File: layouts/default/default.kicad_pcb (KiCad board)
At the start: 2 copper layers, 37 parts

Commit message: Add modular design blocks and placement automation
- Add 8 modular sensor/power blocks in elec/modules/ for better layout
  organization (LIS3DHTR, QMI8658C, HDC2080, power filter, RF matching,
  I2C bus, status LED, NTC temp sensor)
- Add autoplace_v2.py with KiCad Python API and force-directed placement
- Add placement_config.yaml and block_templates.yaml for placement tuning
- Update main design to use modular block architecture
- Clean up old example build artifacts
- Remove unused patch_transformers.py

Co-Authored-By: Claude Opus 4.5 <noreply@anthropic.com>
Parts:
- B1: moved to B.Cu
- C1: value 5.6pF 50V C0G -> 1µF ±10% 50V X5R; footprint Murata_Electronics_GJM1555C1H5R6BB01D:C0402 -> Samsung_Electro_Mechanics_CL10A105KB8NNNC:C0603
- C10: value 1.7pF 50V C0G -> 100nF ±10% 50V X7R; footprint Murata_Electronics_GJM1555C1H1R7BB01D:C0402 -> YAGEO_CC0402KRX7R9BB104:C0402
- C11, C8: value 100nF ±10% 50V X7R -> 4.7µF ±10% 10V X5R; footprint YAGEO_CC0402KRX7R9BB104:C0402 -> Murata_Electronics_GRM155R61A475KEAAD:C0402
- C13: value 1µF ±10% 50V X5R -> 1.7pF 50V C0G; footprint Samsung_Electro_Mechanics_CL10A105KB8NNNC:C0603 -> Murata_Electronics_GJM1555C1H1R7BB01D:C0402
- C15, C16: value 100nF ±10% 50V X7R -> 5.6pF 50V C0G; footprint YAGEO_CC0402KRX7R9BB104:C0402 -> Murata_Electronics_GJM1555C1H5R6BB01D:C0402
- C2: value 5.6pF 50V C0G -> 100nF ±10% 50V X7R; footprint Murata_Electronics_GJM1555C1H5R6BB01D:C0402 -> YAGEO_CC0402KRX7R9BB104:C0402
- C3: value 4.7µF ±10% 10V X5R -> 100nF ±10% 50V X7R; footprint Murata_Electronics_GRM155R61A475KEAAD:C0402 -> YAGEO_CC0402KRX7R9BB104:C0402
- C6: value 4.7µF ±10% 10V X5R -> 22µF ±20% 6.3V X5R; footprint Murata_Electronics_GRM155R61A475KEAAD:C0402 -> YAGEO_CC0603MRX5R5BB226:C0603
- C9: value 22µF ±20% 6.3V X5R -> 100nF ±10% 50V X7R; footprint YAGEO_CC0603MRX5R5BB226:C0603 -> YAGEO_CC0402KRX7R9BB104:C0402
- L5: value 4.3nH 6GHz 750mA 140mΩ -> 4.7µH ±5% 175mA 2.3Ω; footprint Murata_Electronics_LQG15HS4N3S02D:L0402 -> TDK_NLV25T_4R7J_PF:IND-SMD_L2.5-W2.0_NLV25T-390J-PF
- L6: value 4.7µH ±5% 175mA 2.3Ω -> 4.3nH 6GHz 750mA 140mΩ; footprint TDK_NLV25T_4R7J_PF:IND-SMD_L2.5-W2.0_NLV25T-390J-PF -> Murata_Electronics_LQG15HS4N3S02D:L0402
- R1: value 10kΩ ±1% 62.5mW -> 4.7kΩ ±5% 62.5mW; footprint YAGEO_RC0402FR_0710KL:R0402 -> YAGEO_RC0402JR_074K7L:R0402
- R2: value (none) -> 4.7kΩ ±5% 62.5mW; footprint Murata_Electronics_NCP15XH103F03RC:R0402 -> YAGEO_RC0402JR_074K7L:R0402
- R3: value 10kΩ ±1% 62.5mW -> 1kΩ ±5% 62.5mW; footprint YAGEO_RC0402FR_0710KL:R0402 -> YAGEO_RC0402JR_071KL:R0402
- R4: value 1kΩ ±5% 62.5mW -> 10kΩ ±1% 62.5mW; footprint YAGEO_RC0402JR_071KL:R0402 -> YAGEO_RC0402FR_0710KL:R0402
- R5: value 4.7kΩ ±5% 62.5mW -> (none); footprint YAGEO_RC0402JR_074K7L:R0402 -> Murata_Electronics_NCP15XH103F03RC:R0402
- R6: value 4.7kΩ ±5% 62.5mW -> 10kΩ ±1% 62.5mW; footprint YAGEO_RC0402JR_074K7L:R0402 -> YAGEO_RC0402FR_0710KL:R0402
- U3: footprint Texas_Instruments_HDC2080DMBR:WSON-6_L3.0-W3.0-P1.00-TL-EP -> STMicroelectronics_LIS3DHTR:LGA-16_L3.0-W3.0-P0.50-TL
- U4: footprint STMicroelectronics_LIS3DHTR:LGA-16_L3.0-W3.0-P0.50-TL -> Texas_Instruments_HDC2080DMBR:WSON-6_L3.0-W3.0-P1.00-TL-EP
- moved L1 265.3 mm to (126.6, 73.2)
- moved R2 212.1 mm to (30.0, -10.0)
- moved C14 191.8 mm to (144.4, 86.2)
- moved R1 172.6 mm to (30.0, 0.00)
- moved U1 128.7 mm to (104.0, 75.7)
- moved B1 128.3 mm to (103.6, 75.7)
- moved H1 123.0 mm to (103.7, 66.1), turned to 180 degrees
- moved U2 117.3 mm to (68.8, 25.0)
- moved L2 86.0 mm to (70.0, -70.0)
- moved L3 86.0 mm to (70.0, -80.0)
- moved L4 86.0 mm to (70.0, -90.0)
- moved C15 85.4 mm to (80.0, -20.0)
- moved C16 85.4 mm to (80.0, -30.0)
- moved C13 82.5 mm to (80.0, -10.0)
- moved L6 82.5 mm to (80.0, -50.0)
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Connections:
- net footprint-CS-1 renamed footprint-CS
- net footprint-INT2-0 renamed footprint-int2
- C1 pad 1: c_harm-net -> accel-vcc
- C10 pad 1: c_harm-net -> accel-vcc
- C11 pad 1: c5-vcc -> c_vcc_1-vcc
- C12 pad 1: c5-vcc -> c_vcc_1-vcc
- C13 pad 1: c5-vcc -> c_harmonic-net
- C15 pad 1: c5-vcc -> Feed
- C16 pad 1: c5-vcc -> c_harmonic-net
- C2 pad 1: Feed -> accel-vcc
- C3 pad 1: c1-vcc -> accel-vcc
- C4 pad 1: c1-vcc -> accel-vcc
- C5 pad 1: vcc_mcu -> accel-vcc
- C6 pad 1: vcc_mcu -> vbat
- C7 pad 1: c5-vcc -> vcc_mcu
- C8 pad 1: c5-vcc -> vcc_mcu
- C9 pad 1: vbat -> accel-vcc
- H1 pad 1: c1-vcc -> c_vcc_1-vcc
- L2 pad 2: c1-vcc -> c_vcc_1-vcc
- L3 pad 1: c1-vcc -> c_vcc_1-vcc
- L4 pad 1: c1-vcc -> c_vcc_1-vcc
- L4 pad 2: c5-vcc -> accel-vcc
- L5 pad 1: c_harm-net -> RF_OUT
- L5 pad 2: Feed -> c_harmonic-net
- L6 pad 1: RF_OUT -> c_harmonic-net
- L6 pad 2: c_harm-net -> Feed
- R1 pad 1: c1-vcc -> c_vcc_1-vcc
- R1 pad 2: adc_ntc -> i2c_scl
- R2 pad 1: adc_ntc -> c_vcc_1-vcc
- R2 pad 2: gnd -> i2c_sda
- R3 pad 1: c1-vcc -> gpio_in
- R3 pad 2: activation -> A
- R4 pad 1: led_status -> c_vcc_1-vcc
- R4 pad 2: A -> adc_ntc
- R5 pad 1: c1-vcc -> adc_ntc
- R5 pad 2: i2c_sda -> gnd
- R6 pad 1: c1-vcc -> c_vcc_1-vcc
- R6 pad 2: i2c_scl -> activation
- U1 pad 14: footprint-INT2-1 -> accel-int2
- U1 pad 15: INT1 -> int1
- U1 pad 16: led_status -> gpio_in
- U1 pad 19: DRDY_INT -> int_pin
- U2 pad 4: c5-vcc -> accel-vcc
- U3 pad 1: i2c_sda -> accel-vcc
- U3 pad 2: gnd -> accel-net-0
- U3 pad 3: gnd -> accel-net-1
- U3 pad 4: DRDY_INT -> i2c_scl
- U3 pad 5: c5-vcc -> gnd
- U3 pad 6: i2c_scl -> i2c_sda
- U4 pad 1: c5-vcc -> i2c_sda
- U4 pad 2: footprint-net-4 -> gnd
- U4 pad 3: footprint-net-5 -> gnd
- U4 pad 4: i2c_scl -> int_pin
- U4 pad 5: gnd -> accel-vcc
- U4 pad 6: i2c_sda -> i2c_scl
- U5 pad 5: c5-vcc -> accel-vcc
- U5 pad 8: c5-vcc -> accel-vcc
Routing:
- net nrst: track 0.00 -> 17.7 mm
- net swdio: track 0.00 -> 11.2 mm
- net swclk: track 0.00 -> 10.9 mm
- net (no net): track 0.00 -> 10.5 mm

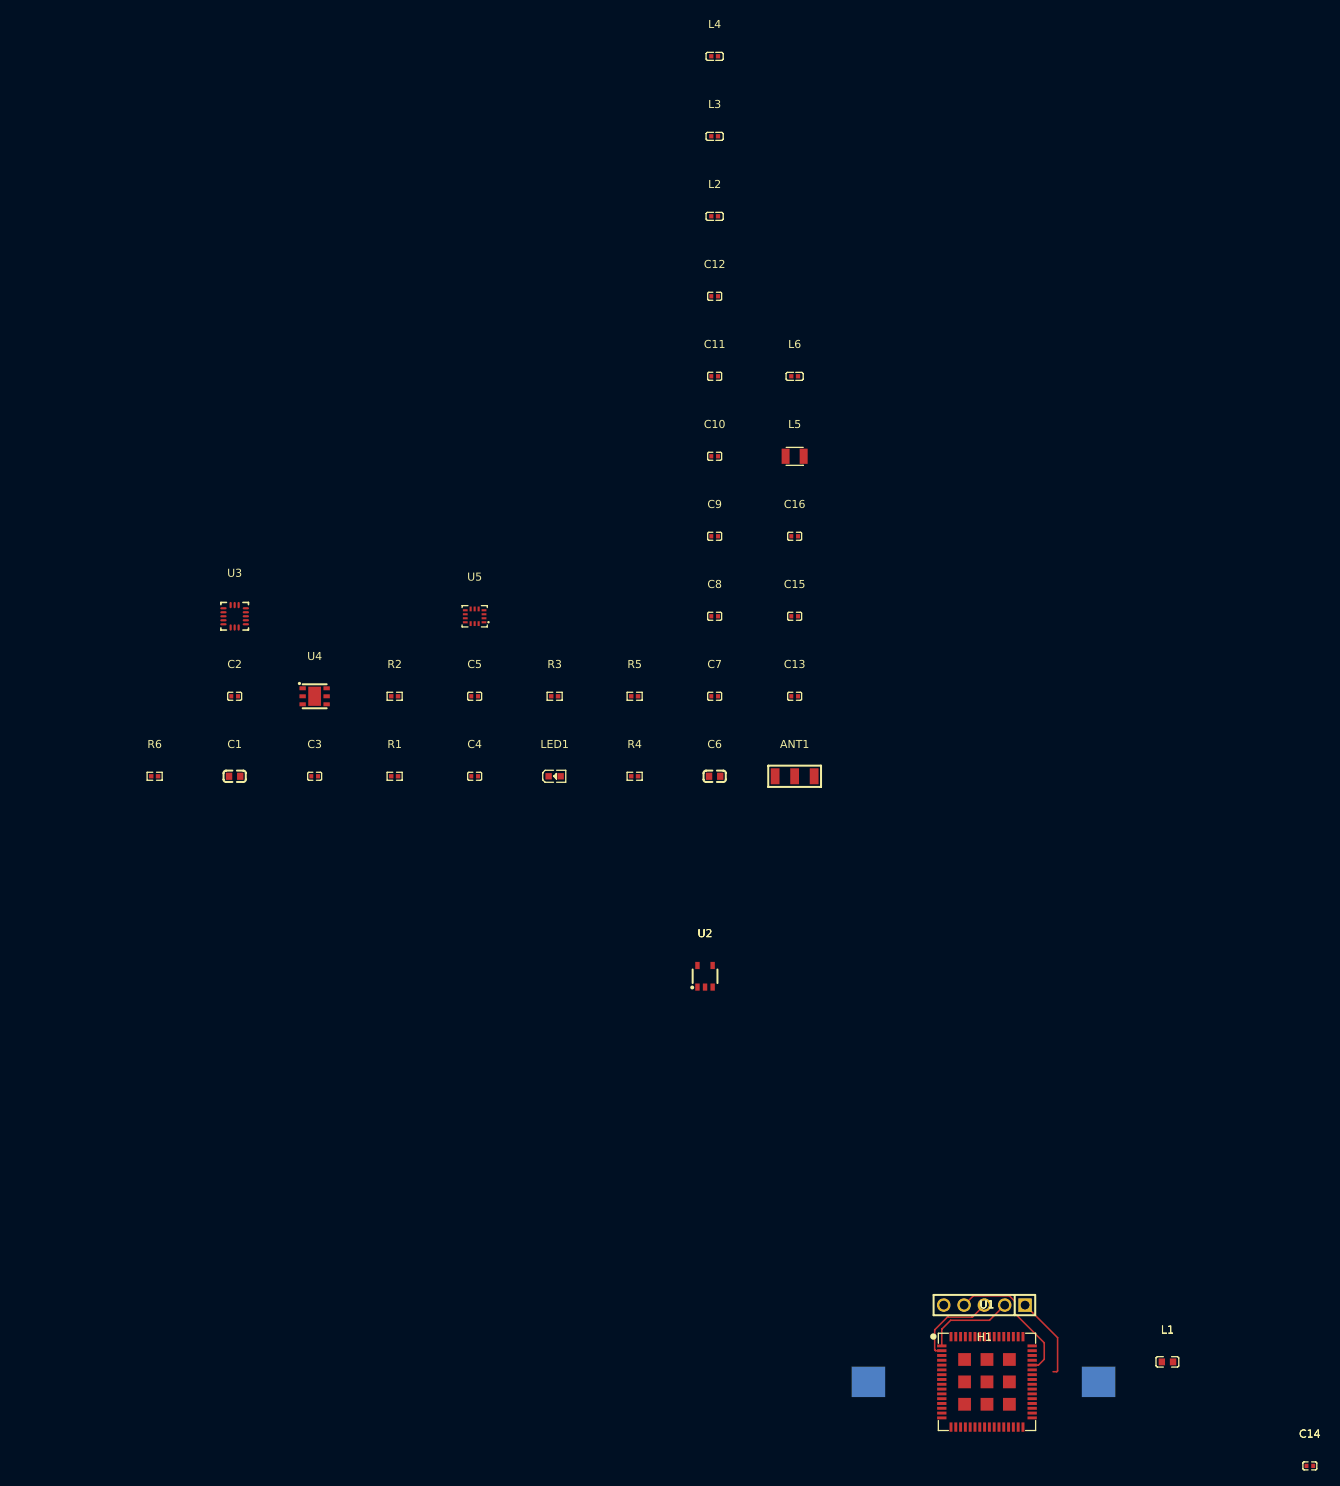
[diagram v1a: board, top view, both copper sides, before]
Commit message: Enhance smart placer with simulated annealing and pre-routing validation
Smart Placer improvements:
- Add simulated annealing refinement (now default) for better wire length optimization
- Add force-directed refinement with improvement safeguard
- Add silkscreen text repositioning to avoid component overlaps
- Significant wire length reductions (e.g., power_filter: 113mm -> 46mm)

Autorouter improvements:
- Add PreRoutingValidator class for pre-flight checks
- Validate unconnected pads, overlapping footprints, unplaced components
- Use pad-based bounds for accurate overlap detection
- Block routing on validation errors with actionable messages

Research:
- Add comprehensive autorouting/autoplacement findings document
- Cover Freerouting Python client, OrthoRoute, DeepPCB, KiCad 9 IPC API
- Document force-directed and simulated annealing algorithms

Cleanup:
- Update .gitignore for DSN/SES files, build artifacts, tools
- Remove stale timestamped build files
- Add parts footprints and symbols

All 10 modules placed and routed successfully.

Co-Authored-By: Claude Opus 4.5 <noreply@anthropic.com>
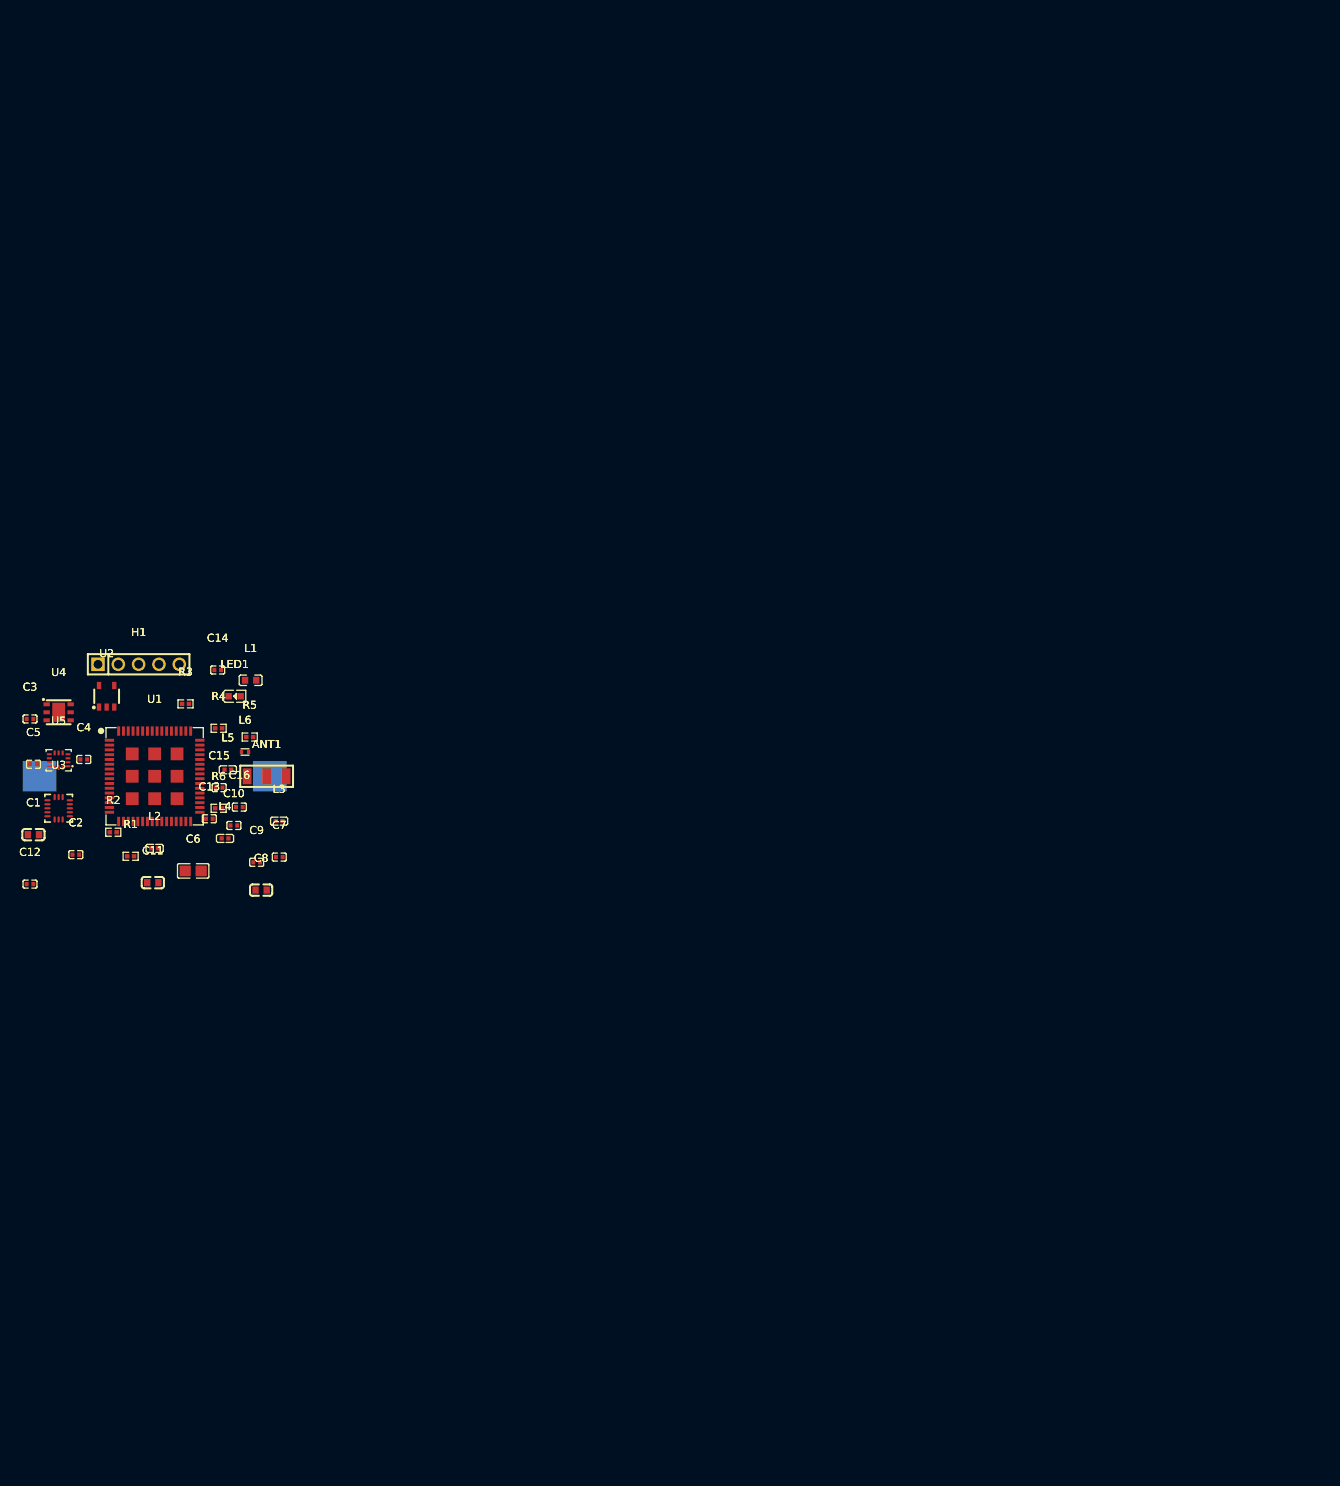
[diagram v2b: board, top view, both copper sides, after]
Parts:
- C1: value 1µF ±10% 50V X5R -> 10µF ±10% 10V X5R; footprint Samsung_Electro_Mechanics_CL10A105KB8NNNC:C0603 -> Samsung_Electro_Mechanics_CL10A106KP8NNNC:C0603
- C10, C12, C14, C2, C3, C4, C5, C7, C9: value 100nF ±10% 50V X7R -> 100nF ±10% 16V X7R; footprint YAGEO_CC0402KRX7R9BB104:C0402 -> Samsung_Electro_Mechanics_CL05B104KO5NNNC:C0402
- C11, C8: value 4.7µF ±10% 10V X5R -> 4.7µF ±10% 16V X5R; footprint Murata_Electronics_GRM155R61A475KEAAD:C0402 -> Samsung_Electro_Mechanics_CL10A475KO8NNNC:C0603
- C13: value 1.7pF 50V C0G -> 3.3pF ±2% 50V C0G; footprint Murata_Electronics_GJM1555C1H1R7BB01D:C0402 -> Murata_Electronics_GCM1555C1H3R3GA16D:C0402
- C15, C16: value 5.6pF 50V C0G -> (none)
- C6: value 22µF ±20% 6.3V X5R -> 22µF ±20% 25V X5R; footprint YAGEO_CC0603MRX5R5BB226:C0603 -> Samsung_Electro_Mechanics_CL21A226MAQNNNE:C0805
- L5: value 4.7µH ±5% 175mA 2.3Ω -> 8.2nH ±5% 3.6GHz 300mA 400mΩ; footprint TDK_NLV25T_4R7J_PF:IND-SMD_L2.5-W2.0_NLV25T-390J-PF -> Sunlord_SDCL1005C8N2JTDF:L0402
- L6: value 4.3nH 6GHz 750mA 140mΩ -> 4.2nH ±2% 1.8A 44mΩ; footprint Murata_Electronics_LQG15HS4N3S02D:L0402 -> Murata_Electronics_LQW15AN4N2G80D:IND-SMD_L1.0-W0.5-2
- R1, R2: value 4.7kΩ ±5% 62.5mW -> 4.7kΩ ±1% 62.5mW; footprint YAGEO_RC0402JR_074K7L:R0402 -> UNI_ROYAL_0402WGF4701TCE:R0402
- R3: value 1kΩ ±5% 62.5mW -> 1kΩ ±1% 62.5mW; footprint YAGEO_RC0402JR_071KL:R0402 -> UNI_ROYAL_0402WGF1001TCE:R0402
- R4, R6: footprint YAGEO_RC0402FR_0710KL:R0402 -> UNI_ROYAL_0402WGF1002TCE:R0402
- moved C14 168.9 mm to (7.88, -13.3)
- moved L1 142.8 mm to (12.0, -12.0)
- moved H1 132.6 mm to (-2.00, -14.0), turned to 0 degrees
- moved U1 128.7 mm to (0.00, 0.00)
- moved B1 128.3 mm to (0.00, 0.00)
- moved L4 115.3 mm to (8.80, 7.76)
- moved C12 112.8 mm to (-15.6, 13.5)
- moved L2 105.6 mm to (0.00, 9.00)
- moved L3 101.4 mm to (15.6, 5.60)
- moved C11 94.5 mm to (-0.23, 13.3)
- moved L6 83.2 mm to (11.3, -3.03)
- moved U2 82.6 mm to (-6.00, -10.0)
- moved L5 81.0 mm to (9.15, -0.82)
- moved C16 77.2 mm to (10.6, 3.85)
- moved C10 75.8 mm to (9.91, 6.15)
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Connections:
- net c_harmonic-net renamed _1
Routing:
- net nrst: track 17.7 -> 0.00 mm
- net swdio: track 11.2 -> 0.00 mm
- net swclk: track 10.9 -> 0.00 mm
- net (no net): track 10.5 -> 0.00 mm
